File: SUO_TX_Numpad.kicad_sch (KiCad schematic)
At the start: 15 parts, among them J1 USB_C_Receptacle_USB2.0_16P, SW1 BOOT, U1 STM32F411CEUx, U2 XC6206PxxxMR-Regulator_Linear, U3 USBLC6-2SC6

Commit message: Added LCSC, but going to switch to 0603 or 0804 components as I want to keep handsoldering an option
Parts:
- C1, C2, C3: value 10uF 16V -> 10uF; LCSC (none) -> C315248
- C4: value 10pF 16V -> 10pF; LCSC (none) -> C32949
- F1: value Fuse 1500mA Fast -> Fuse 1A Fast; LCSC (none) -> C424347
- J1: LCSC (none) -> C2765186
- LED22: LCSC (none) -> C5242955
- R1, R2: LCSC (none) -> C105872
- R3, R4: LCSC (none) -> C60490
- SW1: LCSC (none) -> C221676
- U1: LCSC (none) -> C60420
- U3: LCSC (none) -> C7519
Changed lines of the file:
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@@
+			)
+		)
+		(property "LCSC" "C60490"
+			(at 46.99 41.91 90)
+			(effects
+				(font
+					(size 1.27 1.27)
+				)
+				(hide yes)
 			)
 		)
@@
 		(fields_autoplaced yes)
 		(property "Reference" "C1"
-			(at 147.32 90.17 0)
+			(at 147.32 90.1699 0)
 			(effects
 				(font
@@
 			)
 		)
-		(property "Value" "10uF 16V"
-			(at 147.32 92.71 0)
+		(property "Value" "10uF"
+			(at 147.32 92.7099 0)
 			(effects
 				(font
@@
 			)
 		)
+		(property "LCSC" "C315248"
+			(at 143.51 91.44 0)
+			(effects
+				(font
+					(size 1.27 1.27)
+				)
+				(hide yes)
+			)
+		)
 		(pin "1"
 		)
@@
 			)
 		)
-		(property "Value" "Fuse 1500mA Fast"
+		(property "Value" "Fuse 1A Fast"
 			(at 118.11 68.58 0)
 			(effects
@@
 			)
 		)
+		(property "LCSC" "C424347"
+			(at 118.11 71.12 0)
+			(effects
+				(font
+					(size 1.27 1.27)
+				)
+				(hide yes)
+			)
+		)
 		(pin "2"
 		)
@@
 			)
 		)
+		(property "LCSC" "C5242955"
+			(at 236.22 57.15 0)
+			(effects
+				(font
+					(size 1.27 1.27)
+				)
+				(hide yes)
+			)
+		)
 		(pin "4"
 		)
@@
 			)
 		)
+		(property "LCSC" "C105872"
+			(at 139.7 97.79 90)
+			(effects
+				(font
+					(size 1.27 1.27)
+				)
+				(hide yes)
+			)
+		)
 		(pin "1"
 		)
@@
 			)
 		)
+		(property "LCSC" "C60420"
+			(at 60.96 82.55 0)
+			(effects
+				(font
+					(size 1.27 1.27)
+				)
+				(hide yes)
+			)
+		)
 		(pin "18"
 		)
@@
 		(fields_autoplaced yes)
 		(property "Reference" "C3"
-			(at 135.89 41.91 0)
+			(at 135.89 41.9099 0)
 			(effects
 				(font
@@
 			)
 		)
-		(property "Value" "10uF 16V"
-			(at 135.89 44.45 0)
+		(property "Value" "10uF"
+			(at 135.89 44.4499 0)
 			(effects
 				(font
@@
 			)
 		)
+		(property "LCSC" "C315248"
+			(at 132.08 43.18 0)
+			(effects
+				(font
+					(size 1.27 1.27)
+				)
+				(hide yes)
+			)
+		)
 		(pin "1"
 		)
@@
 			)
 		)
-		(property "Value" "10pF 16V"
+		(property "Value" "10pF"
 			(at 38.1 121.9199 0)
 			(effects
@@
 			)
 		)
+		(property "LCSC" "C32949"
+			(at 34.29 120.65 0)
+			(effects
+				(font
+					(size 1.27 1.27)
+				)
+				(hide yes)
+			)
+		)
 		(pin "1"
 		)
@@
 		(fields_autoplaced yes)
 		(property "Reference" "C2"
-			(at 106.68 41.91 0)
+			(at 106.68 41.9099 0)
 			(effects
 				(font
@@
 			)
 		)
-		(property "Value" "10uF 16V"
-			(at 106.68 44.45 0)
+		(property "Value" "10uF"
+			(at 106.68 44.4499 0)
 			(effects
 				(font
@@
 			)
 		)
+		(property "LCSC" "C315248"
+			(at 102.87 43.18 0)
+			(effects
+				(font
+					(size 1.27 1.27)
+				)
+				(hide yes)
+			)
+		)
 		(pin "1"
 		)
@@
 			)
 		)
+		(property "LCSC" "C221676"
+			(at 36.83 36.83 0)
+			(effects
+				(font
+					(size 1.27 1.27)
+				)
+				(hide yes)
+			)
+		)
 		(pin "2"
 		)
@@
 			)
 		)
+		(property "LCSC" "C7519"
+			(at 171.45 53.34 0)
+			(effects
+				(font
+					(size 1.27 1.27)
+				)
+				(hide yes)
+			)
+		)
 		(pin "1"
 		)
@@
 			)
 		)
+		(property "LCSC" "C2765186"
+			(at 115.57 105.41 0)
+			(effects
+				(font
+					(size 1.27 1.27)
+				)
+				(hide yes)
+			)
+		)
 		(pin "B1"
 		)
@@
 			)
 		)
+		(property "LCSC" "C60490"
+			(at 35.56 52.07 90)
+			(effects
+				(font
+					(size 1.27 1.27)
+				)
+				(hide yes)
+			)
+		)
 		(pin "1"
 		)
@@
 			(effects
 				(font
+					(size 1.27 1.27)
+				)
+				(hide yes)
+			)
+		)
+		(property "LCSC" "C105872"
+			(at 134.62 95.25 90)
+			(effects
+				(font

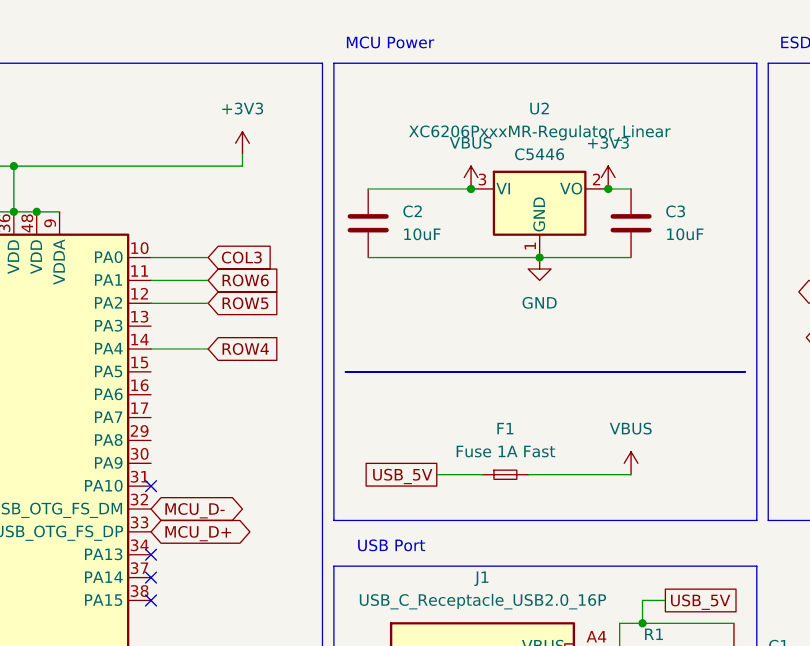
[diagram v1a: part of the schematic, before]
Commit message: Switched to 0805 for R C and SOD-123 for Diodes
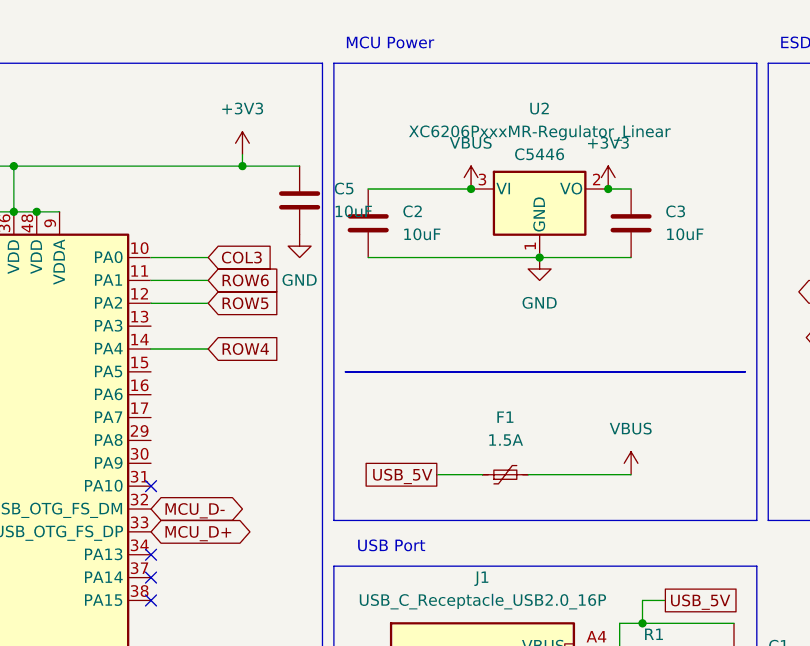
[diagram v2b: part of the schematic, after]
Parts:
- removed F1: Fuse 1A Fast, Fuse:Fuse_0402_1005Metric_Pad0.77x0.64mm_HandSolder, symbol Device:Fuse_Small
- added C5: 10uF, Capacitor_SMD:C_0805_2012Metric_Pad1.18x1.45mm_HandSolder, symbol Device:C
- added F1: 1.5A, Fuse:Fuse_1206_3216Metric_Pad1.42x1.75mm_HandSolder, symbol Device:Polyfuse_Small
- C1, C2, C3, C4: footprint Capacitor_SMD:C_0402_1005Metric_Pad0.74x0.62mm_HandSolder -> Capacitor_SMD:C_0805_2012Metric_Pad1.18x1.45mm_HandSolder
- R1, R2, R3, R4: footprint Resistor_SMD:R_0402_1005Metric_Pad0.72x0.64mm_HandSolder -> Resistor_SMD:R_0805_2012Metric_Pad1.20x1.40mm_HandSolder
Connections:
- net +3V3: now also C5.1
- net GND: now also C5.2
- net USB_5V: now also F1.1
- net VBUS: now also F1.2
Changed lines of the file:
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@@
 		(color 0 0 0 0)
 	)
+	(junction
+		(at 88.9 36.83)
+		(diameter 0)
+		(color 0 0 0 0)
+	)
 	(no_connect
 		(at 243.84 57.15)
@@
 	(wire
 		(pts
+			(xy 95.25 36.83) (xy 88.9 36.83)
+		)
+		(stroke
+			(width 0)
+			(type default)
+		)
+	)
+	(wire
+		(pts
 			(xy 130.81 90.17) (xy 130.81 87.63)
 		)
@@
 	)
 	(symbol
+		(lib_id "Device:Polyfuse_Small")
+		(at 118.11 71.12 90)
+		(unit 1)
+		(exclude_from_sim no)
+		(in_bom yes)
+		(on_board yes)
+		(dnp no)
+		(fields_autoplaced yes)
+		(property "Reference" "F1"
+			(at 118.11 64.77 90)
+			(effects
+				(font
+					(size 1.27 1.27)
+				)
+			)
+		)
+		(property "Value" "1.5A"
+			(at 118.11 67.31 90)
+			(effects
+				(font
+					(size 1.27 1.27)
+				)
+			)
+		)
+		(property "Footprint" "Fuse:Fuse_1206_3216Metric_Pad1.42x1.75mm_HandSolder"
+			(at 123.19 69.85 0)
+			(effects
+				(font
+					(size 1.27 1.27)
+				)
+				(justify left)
+				(hide yes)
+			)
+		)
+		(property "Datasheet" "https://www.lcsc.com/datasheet/C28326719.pdf?spm=wm.sxq.inf.ggs___wm.ssy.bg.12.xh&lcsc_vid=E1gIUlwEFVkPV1UEQVZbBQADQVgMBlQEQllcBQYFFFExVlNRQ1NaUF1XRlNeUjsOAxUeFF5JWBYZEEoKFBINSQcJGk4dAgUUFAk%3D"
+			(at 118.11 71.12 0)
+			(effects
+				(font
+					(size 1.27 1.27)
+				)
+				(hide yes)
+			)
+		)
+		(property "Description" "Resettable fuse, polymeric positive temperature coefficient, small symbol"
+			(at 118.11 71.12 0)
+			(effects
+				(font
+					(size 1.27 1.27)
+				)
+				(hide yes)
+			)
+		)
+		(property "LCSC" "C28326719"
+			(at 118.11 71.12 90)
+			(effects
+				(font
+					(size 1.27 1.27)
+				)
+				(hide yes)
+			)
+		)
+		(pin "2"
+		)
+		(pin "1"
+		)
+		(instances
+			(project ""
+				(path "/4f42914a-d4c6-4461-b1c3-be7726ab46dc"
+					(reference "F1")
+					(unit 1)
+				)
+			)
+		)
+	)
+	(symbol
 		(lib_id "Device:R")
 		(at 46.99 41.91 90)
@@
 			)
 		)
-		(property "Footprint" "Resistor_SMD:R_0402_1005Metric_Pad0.72x0.64mm_HandSolder"
+		(property "Footprint" "Resistor_SMD:R_0805_2012Metric_Pad1.20x1.40mm_HandSolder"
 			(at 46.99 43.688 90)
 			(effects
@@
 			)
 		)
-		(property "Footprint" "Capacitor_SMD:C_0402_1005Metric_Pad0.74x0.62mm_HandSolder"
+		(property "Footprint" "Capacitor_SMD:C_0805_2012Metric_Pad1.18x1.45mm_HandSolder"
 			(at 144.4752 95.25 0)
 			(effects
@@
 	)
 	(symbol
-		(lib_id "Device:Fuse_Small")
-		(at 118.11 71.12 0)
-		(unit 1)
-		(exclude_from_sim no)
-		(in_bom yes)
-		(on_board yes)
-		(dnp no)
-		(property "Reference" "F1"
-			(at 118.11 66.04 0)
-			(effects
-				(font
-					(size 1.27 1.27)
-				)
-			)
-		)
-		(property "Value" "Fuse 1A Fast"
-			(at 118.11 68.58 0)
-			(effects
-				(font
-					(size 1.27 1.27)
-				)
-			)
-		)
-		(property "Footprint" "Fuse:Fuse_0402_1005Metric_Pad0.77x0.64mm_HandSolder"
-			(at 118.11 71.12 0)
-			(effects
-				(font
-					(size 1.27 1.27)
-				)
-				(hide yes)
-			)
-		)
-		(property "Datasheet" ""
-			(at 118.11 71.12 0)
-			(effects
-				(font
-					(size 1.27 1.27)
-				)
-				(hide yes)
-			)
-		)
-		(property "Description" ""
-			(at 118.11 71.12 0)
-			(effects
-				(font
-					(size 1.27 1.27)
-				)
-			)
-		)
-		(property "KiLib_Generator" "SMD_2terminal_chip_molded"
-			(at 118.11 71.12 0)
-			(effects
-				(font
-					(size 1.27 1.27)
-				)
-				(hide yes)
-			)
-		)
-		(property "LCSC" "C424347"
-			(at 118.11 71.12 0)
-			(effects
-				(font
-					(size 1.27 1.27)
-				)
-				(hide yes)
-			)
-		)
-		(pin "2"
-		)
-		(pin "1"
-		)
-		(instances
-			(project "SUO_TX_Numpad"
-				(path "/4f42914a-d4c6-4461-b1c3-be7726ab46dc"
-					(reference "F1")
-					(unit 1)
-				)
-			)
-		)
-	)
-	(symbol
 		(lib_id "LED:SK6812MINI-E")
 		(at 236.22 57.15 0)
@@
 			)
 		)
-		(property "Footprint" "Resistor_SMD:R_0402_1005Metric_Pad0.72x0.64mm_HandSolder"
+		(property "Footprint" "Resistor_SMD:R_0805_2012Metric_Pad1.20x1.40mm_HandSolder"
 			(at 139.7 99.568 90)
 			(effects
@@
 	)
 	(symbol
+		(lib_id "Device:C")
+		(at 95.25 40.64 0)
+		(unit 1)
+		(exclude_from_sim no)
+		(in_bom yes)
+		(on_board yes)
+		(dnp no)
+		(fields_autoplaced yes)
+		(property "Reference" "C5"
+			(at 99.06 39.3699 0)
+			(effects
+				(font
+					(size 1.27 1.27)
+				)
+				(justify left)
+			)
+		)
+		(property "Value" "10uF"
+			(at 99.06 41.9099 0)
+			(effects
+				(font
+					(size 1.27 1.27)
+				)
+				(justify left)
+			)
+		)
+		(property "Footprint" "Capacitor_SMD:C_0805_2012Metric_Pad1.18x1.45mm_HandSolder"
+			(at 96.2152 44.45 0)
+			(effects
+				(font
+					(size 1.27 1.27)
+				)
+				(hide yes)
+			)
+		)
+		(property "Datasheet" ""
+			(at 95.25 40.64 0)
+			(effects
+				(font
+					(size 1.27 1.27)
+				)
+				(hide yes)
+			)
+		)
+		(property "Description" ""
+			(at 95.25 40.64 0)
+			(effects
+				(font
+					(size 1.27 1.27)
+				)
+			)
+		)
+		(property "KiLib_Generator" "SMD_2terminal_chip_molded"
+			(at 95.25 40.64 0)
+			(effects
+				(font
+					(size 1.27 1.27)
+				)
+				(hide yes)
+			)
+		)
+		(property "LCSC" "C315248"
+			(at 95.25 40.64 0)
+			(effects
+				(font
+					(size 1.27 1.27)
+				)
+				(hide yes)
+			)
+		)
+		(pin "1"
+		)
+		(pin "2"
+		)
+		(instances
+			(project "SUO_TX_Numpad"
+				(path "/4f42914a-d4c6-4461-b1c3-be7726ab46dc"
+					(reference "C5")
+					(unit 1)
+				)
+			)
+		)
+	)
+	(symbol
 		(lib_id "MCU_ST_STM32F4:STM32F411CEUx")
 		(at 60.96 82.55 0)
@@
 			)
 		)
-		(property "Footprint" "Capacitor_SMD:C_0402_1005Metric_Pad0.74x0.62mm_HandSolder"
+		(property "Footprint" "Capacitor_SMD:C_0805_2012Metric_Pad1.18x1.45mm_HandSolder"
 			(at 133.0452 46.99 0)
 			(effects
@@
 			)
 		)
-		(property "Footprint" "Capacitor_SMD:C_0402_1005Metric_Pad0.74x0.62mm_HandSolder"
+		(property "Footprint" "Capacitor_SMD:C_0805_2012Metric_Pad1.18x1.45mm_HandSolder"
 			(at 35.2552 124.46 0)
 			(effects
@@
 			)
 		)
-		(property "Footprint" "Capacitor_SMD:C_0402_1005Metric_Pad0.74x0.62mm_HandSolder"
+		(property "Footprint" "Capacitor_SMD:C_0805_2012Metric_Pad1.18x1.45mm_HandSolder"
 			(at 103.8352 46.99 0)
 			(effects
@@
 			)
 		)
-		(property "Footprint" "Resistor_SMD:R_0402_1005Metric_Pad0.72x0.64mm_HandSolder"
+		(property "Footprint" "Resistor_SMD:R_0805_2012Metric_Pad1.20x1.40mm_HandSolder"
 			(at 35.56 53.848 90)
 			(effects
@@
 			)
 		)
-		(property "Footprint" "Resistor_SMD:R_0402_1005Metric_Pad0.72x0.64mm_HandSolder"
+		(property "Footprint" "Resistor_SMD:R_0805_2012Metric_Pad1.20x1.40mm_HandSolder"
 			(at 134.62 97.028 90)
 			(effects
@@
 					(unit 1)
 				)
+			)
+		)
+	)
+	(symbol
+		(lib_id "power:GND")
+		(at 95.25 44.45 0)
+		(unit 1)
+		(exclude_from_sim no)
+		(in_bom yes)
+		(on_board yes)
+		(dnp no)
+		(fields_autoplaced yes)
+		(property "Reference" "#PWR034"
+			(at 95.25 50.8 0)
+			(effects
+				(font
+					(size 1.27 1.27)
+				)
+				(hide yes)
+			)
+		)
+		(property "Value" "GND"
+			(at 95.25 49.53 0)
+			(effects
+				(font
+					(size 1.27 1.27)
+				)
+			)
+		)
+		(property "Footprint" ""
+			(at 95.25 44.45 0)
+			(effects
+				(font
+					(size 1.27 1.27)
+				)
+				(hide yes)
+			)
+		)
+		(property "Datasheet" ""
+			(at 95.25 44.45 0)
+			(effects
+				(font
+					(size 1.27 1.27)
+				)
+				(hide yes)
+			)
+		)
+		(property "Description" ""
+			(at 95.25 44.45 0)
+			(effects
+				(font
+					(size 1.27 1.27)
+				)
+			)
+		)
+		(pin "1"
+		)
+		(instances
+			(project "SUO_TX_Numpad"
+				(path "/4f42914a-d4c6-4461-b1c3-be7726ab46dc"
+					(reference "#PWR034")
+					(unit 1)
+				)

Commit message: Updated BOM
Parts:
- C1, C2, C3, C5: LCSC C315248 -> C49010152
- C4: LCSC C32949 -> C5137467
- R1, R2: LCSC C105872 -> C2930296
- R3, R4: LCSC C60490 -> C2930231
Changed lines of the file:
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@@
 	)
 	(symbol
+		(lib_name "R_1")
 		(lib_id "Device:R")
 		(at 46.99 41.91 90)
@@
 			)
 		)
-		(property "LCSC" "C60490"
+		(property "LCSC" "C2930231"
 			(at 46.99 41.91 90)
 			(effects
@@
 			)
 		)
-		(property "LCSC" "C315248"
+		(property "LCSC" "C49010152"
 			(at 143.51 91.44 0)
 			(effects
@@
 			)
 		)
-		(property "LCSC" "C105872"
+		(property "LCSC" "C2930296"
 			(at 139.7 97.79 90)
 			(effects
@@
 			)
 		)
-		(property "LCSC" "C315248"
+		(property "LCSC" "C49010152"
 			(at 95.25 40.64 0)
 			(effects
@@
 			)
 		)
-		(property "LCSC" "C315248"
+		(property "LCSC" "C49010152"
 			(at 132.08 43.18 0)
 			(effects
@@
 			)
 		)
-		(property "LCSC" "C32949"
+		(property "LCSC" "C5137467"
 			(at 34.29 120.65 0)
 			(effects
@@
 			)
 		)
-		(property "LCSC" "C315248"
+		(property "LCSC" "C49010152"
 			(at 102.87 43.18 0)
 			(effects
@@
 			)
 		)
-		(property "LCSC" "C60490"
+		(property "LCSC" "C2930231"
 			(at 35.56 52.07 90)
 			(effects
@@
 			)
 		)
-		(property "LCSC" "C105872"
+		(property "LCSC" "C2930296"
 			(at 134.62 95.25 90)
 			(effects

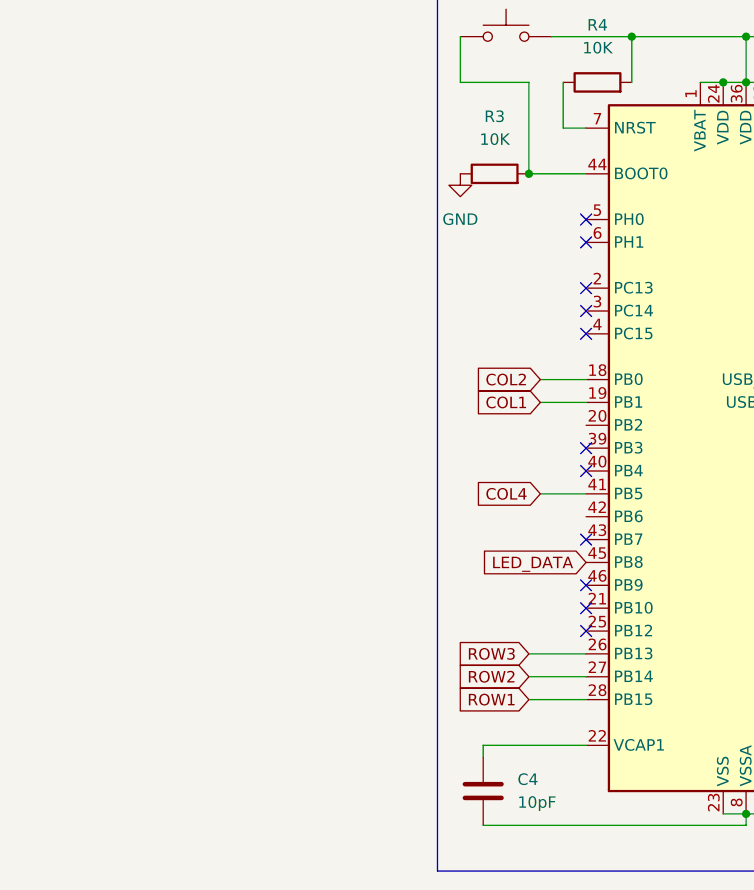
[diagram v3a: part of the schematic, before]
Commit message: Fixed VCAP1 Value to 4.7 uF, added XTAL 8 MHz
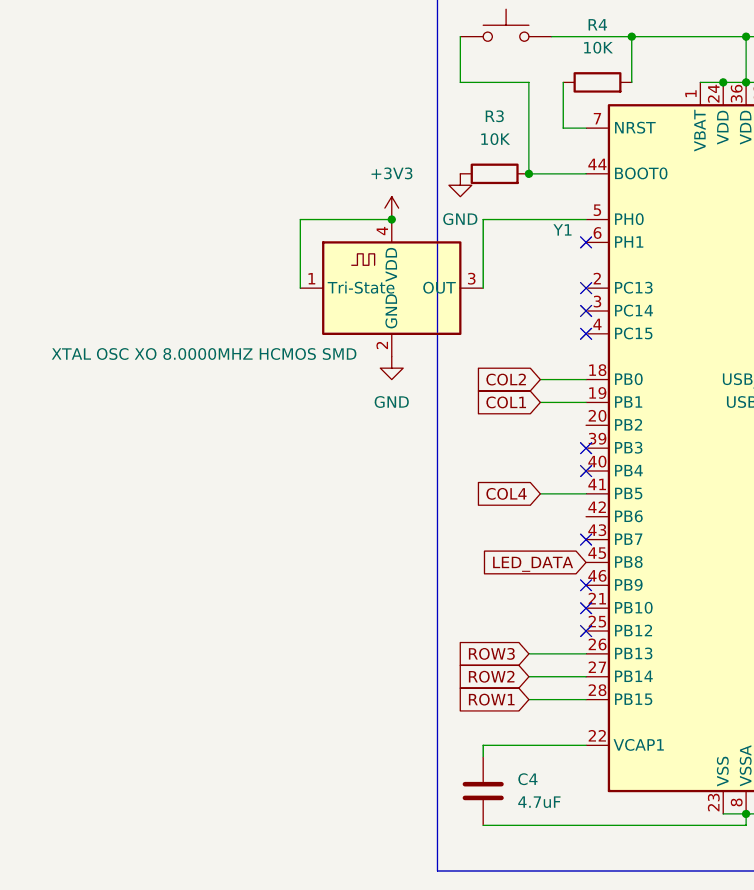
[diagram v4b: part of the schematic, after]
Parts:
- added Y1: XTAL OSC XO 8.0000MHZ HCMOS SMD, Oscillator:Oscillator_SMD_ECS_2520MV-xxx-xx-4Pin_2.5x2.0mm, symbol Oscillator:ECS-2520MV-xxx-xx
- C4: value 10pF -> 4.7uF; DigiKey (none) -> LMK212B7475KG-T; LCSC C5137467 -> C277499
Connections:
- net +3V3: now also Y1.1 (Tri-State), Y1.4 (VDD)
- net GND: now also Y1.2 (GND)
- net at U1.5 (PH0): now also Y1.3 (OUT)
- no-connect marks 19 -> 18
